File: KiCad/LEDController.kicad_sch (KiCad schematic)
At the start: 40 parts, among them J1 Conn_01x05, J2 UART, J3 JTAG, J5 USB_C_Receptacle_USB2.0_16P, J6 Conn_01x03, J7 VDD, J8 GND, J9 Conn_01x14, Q1 IRLZ44N, Q2 IRLZ44N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

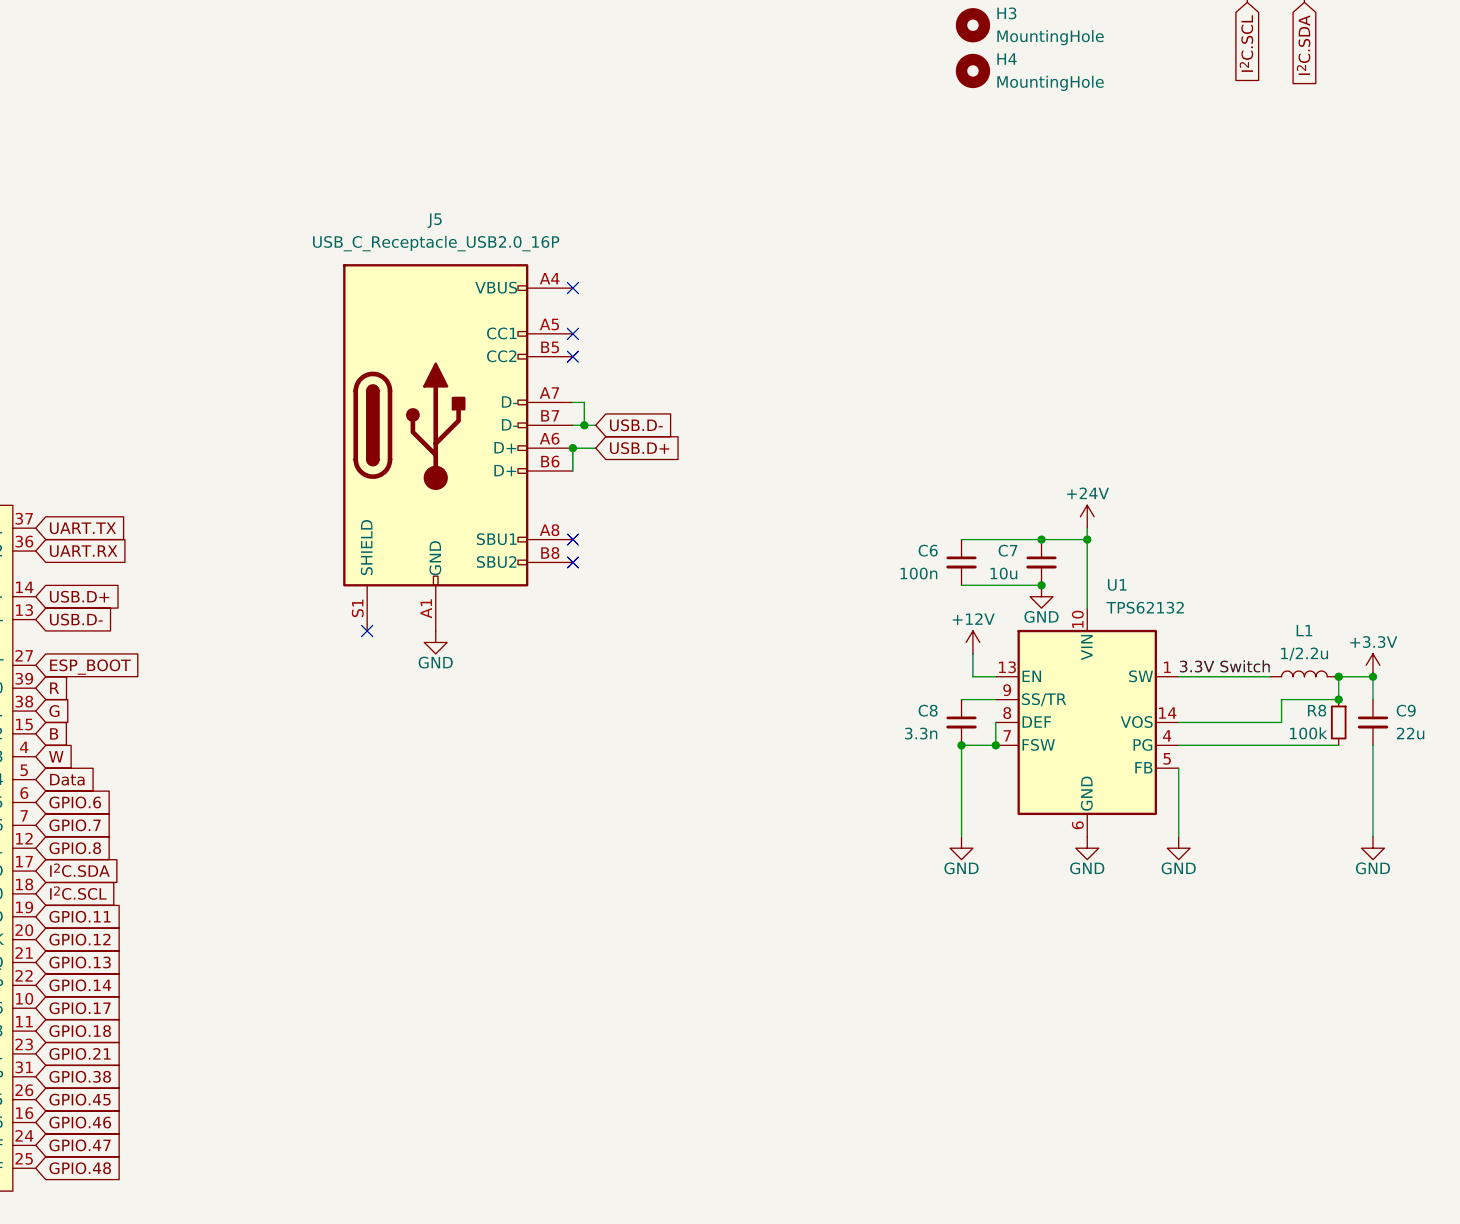
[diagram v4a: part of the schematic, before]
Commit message: add different buck converter
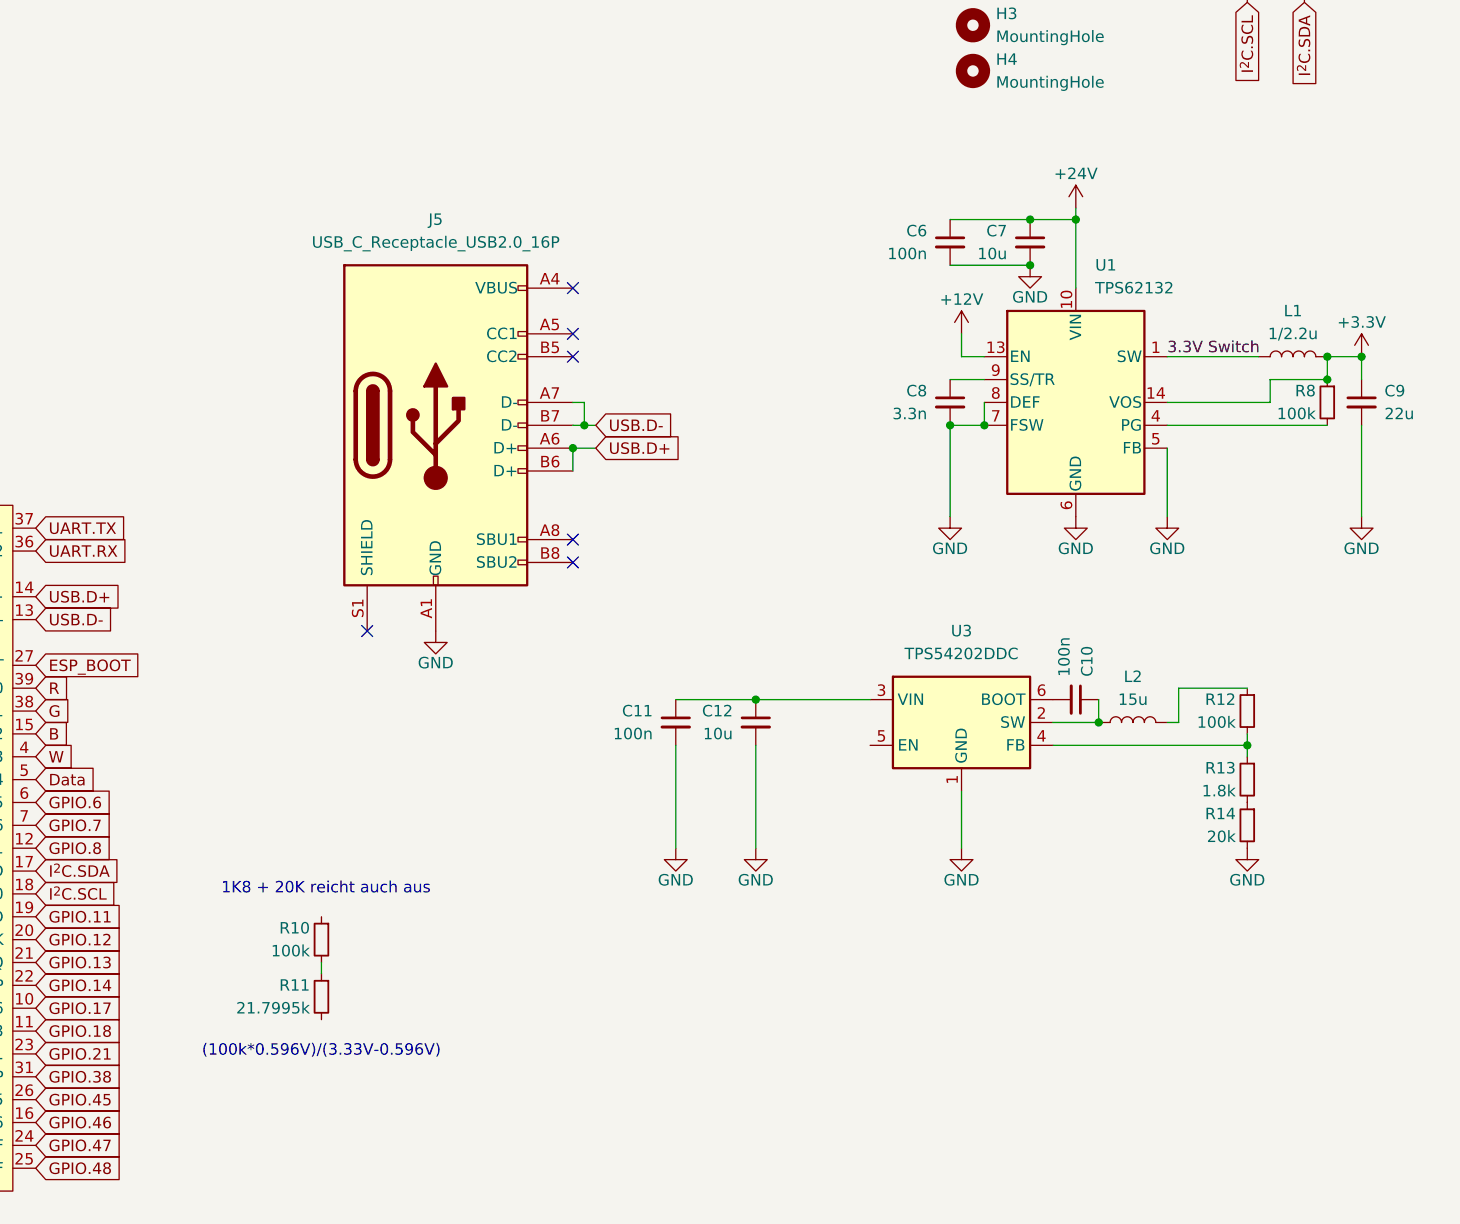
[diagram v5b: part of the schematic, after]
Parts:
- added C10, C11: 100n, Capacitor_SMD:C_0805_2012Metric_Pad1.18x1.45mm_HandSolder, symbol Device:C_Small
- added C12: 10u, Capacitor_SMD:C_1210_3225Metric_Pad1.33x2.70mm_HandSolder, symbol Device:C_Small
- added L2: 15u, Inductor_SMD:L_APV_ANR4026, symbol Device:L
- added R10, R12: 100k, Resistor_SMD:R_0805_2012Metric_Pad1.20x1.40mm_HandSolder, symbol Device:R_Small
- added R11: 21.7995k, Resistor_SMD:R_0805_2012Metric_Pad1.20x1.40mm_HandSolder, symbol Device:R_Small
- added R13: 1.8k, Resistor_SMD:R_0805_2012Metric_Pad1.20x1.40mm_HandSolder, symbol Device:R_Small
- added R14: 20k, Resistor_SMD:R_0805_2012Metric_Pad1.20x1.40mm_HandSolder, symbol Device:R_Small
- added U3: TPS54202DDC, Package_TO_SOT_SMD:SOT-23-6, symbol Regulator_Switching:TPS54202DDC
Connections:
- net GND: now also C11.2, C12.2, R14.2, U3.1 (GND)
- new net: C11.1, C12.1, U3.3 (VIN)
- new net: R13.2, R14.1
- new net: C10.1, L2.1, U3.2 (SW)
- new net: C10.2, U3.6 (BOOT)
- new net: R10.2, R11.1
- new net: L2.2, R12.1
- new net: R12.2, R13.1, U3.4 (FB)
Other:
- note added: "(100k*0.596V)/(3.33V-0.596V)"
- note added: "1K8 + 20K reicht auch aus"
- moved on the sheet: C6, C7, C8, C9, L1, R8, U1

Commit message: rearrange again, route
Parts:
- removed C6: 100n, Capacitor_SMD:C_0805_2012Metric_Pad1.18x1.45mm_HandSolder, symbol Device:C_Small
- removed C7: 10u, Capacitor_SMD:C_1210_3225Metric_Pad1.33x2.70mm_HandSolder, symbol Device:C_Small
- removed C8: 3.3n, Capacitor_SMD:C_0805_2012Metric_Pad1.18x1.45mm_HandSolder, symbol Device:C_Small
- removed C9: 22u, Capacitor_SMD:C_0805_2012Metric_Pad1.18x1.45mm_HandSolder, symbol Device:C_Small
- removed L1: 1/2.2u, Inductor_SMD:L_APV_ANR4026, symbol Device:L
- removed R8: 100k, Resistor_SMD:R_0805_2012Metric_Pad1.20x1.40mm_HandSolder, symbol Device:R_Small
- removed U1: TPS62132, Package_DFN_QFN:VQFN-16-1EP_3x3mm_P0.5mm_EP1.68x1.68mm_ThermalVias, symbol Regulator_Switching:TPS62132
- added C13, C14, C15: 10u, Capacitor_SMD:C_1210_3225Metric_Pad1.33x2.70mm_HandSolder, symbol Device:C_Small
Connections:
- net +24V: now also C11.1, C12.1, U3.3 (VIN)
- net +3.3V: now also L2.2, R12.1, C13.1, C14.1, C15.1
- net GND: now also C13.2, C14.2, C15.2
- no-connect marks 8 -> 9
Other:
- moved on the sheet: C10, C11, C12, L2, R12, R13, R14, U3

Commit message: .
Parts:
- SW2: value ENABLE -> EN
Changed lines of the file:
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@@
 			)
 		)
-		(property "Value" "ENABLE"
+		(property "Value" "EN"
 			(at 264.16 19.05 0)
 			(effects

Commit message: add led
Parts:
- removed C13: 10u, Capacitor_SMD:C_1210_3225Metric_Pad1.33x2.70mm_HandSolder, symbol Device:C_Small
- added D1: LED, symbol Device:LED
- added R8: 100, Resistor_SMD:R_0805_2012Metric_Pad1.20x1.40mm_HandSolder, symbol Device:R_Small
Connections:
- net +3.3V: now also J9.1 (Pin_1)
- net GND: now also J9.2 (Pin_2), D1.1 (K)
- net GPIO.6: now also R8.2; no longer J9.1 (Pin_1), U2.6 (GPIO6/TOUCH6/ADC1_CH5)
- net GPIO.7: no longer names the net of U2.7 (GPIO7/TOUCH7/ADC1_CH6)
- net GPIO.7: no longer J9.2 (Pin_2)
- new net: D1.2 (A), R8.1
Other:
- moved on the sheet: J9
